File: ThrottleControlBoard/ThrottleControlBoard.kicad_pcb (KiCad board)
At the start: 2 copper layers, 95.1 x 65.7 mm, 48 parts, among them J1 BTS7960 module, J10 Conn_02x25_Odd_Even, J2 e-Throttle, J3 Conn_01x14, J4 TB TPS, J5 5V, J6 Conn_02x25_Odd_Even, J7 Conn_02x25_Odd_Even, SW2 SW_SPDT, U1 PCA9685PW

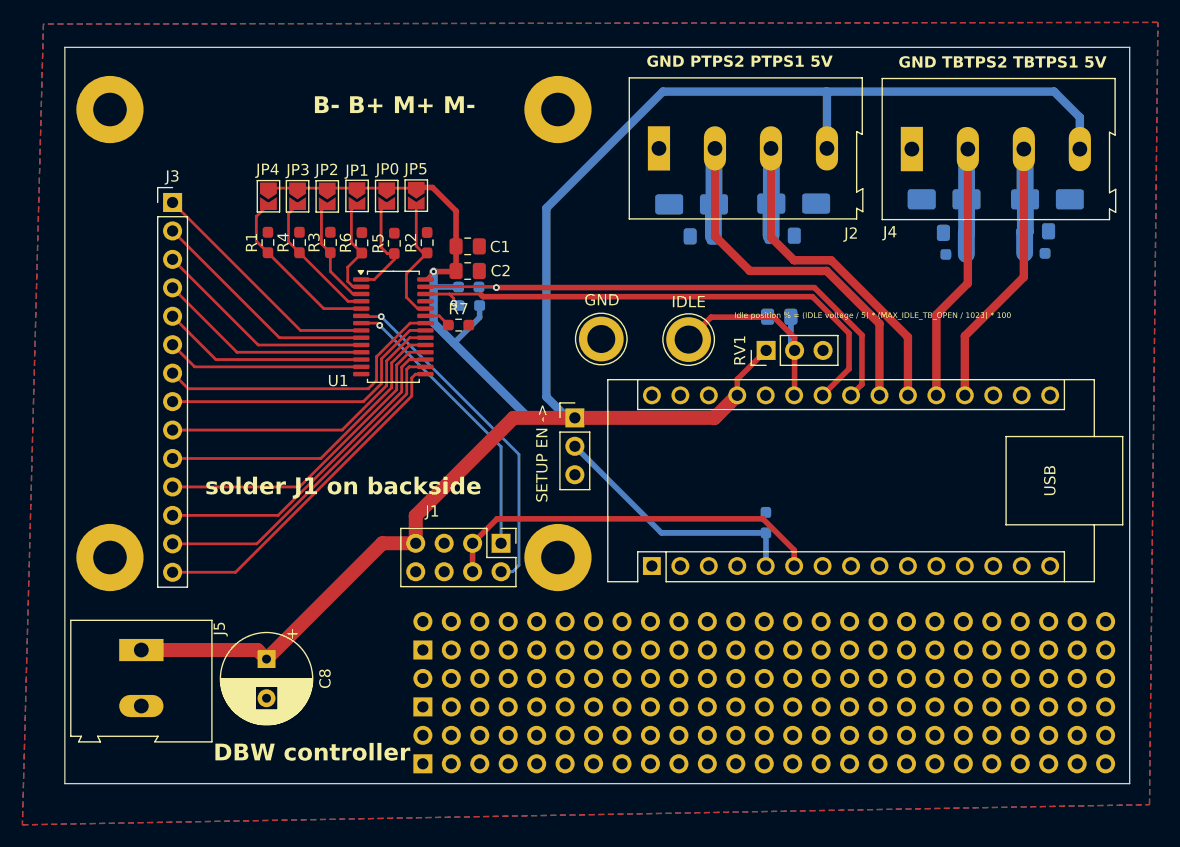
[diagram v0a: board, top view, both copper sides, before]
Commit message: DRC and vias fixed
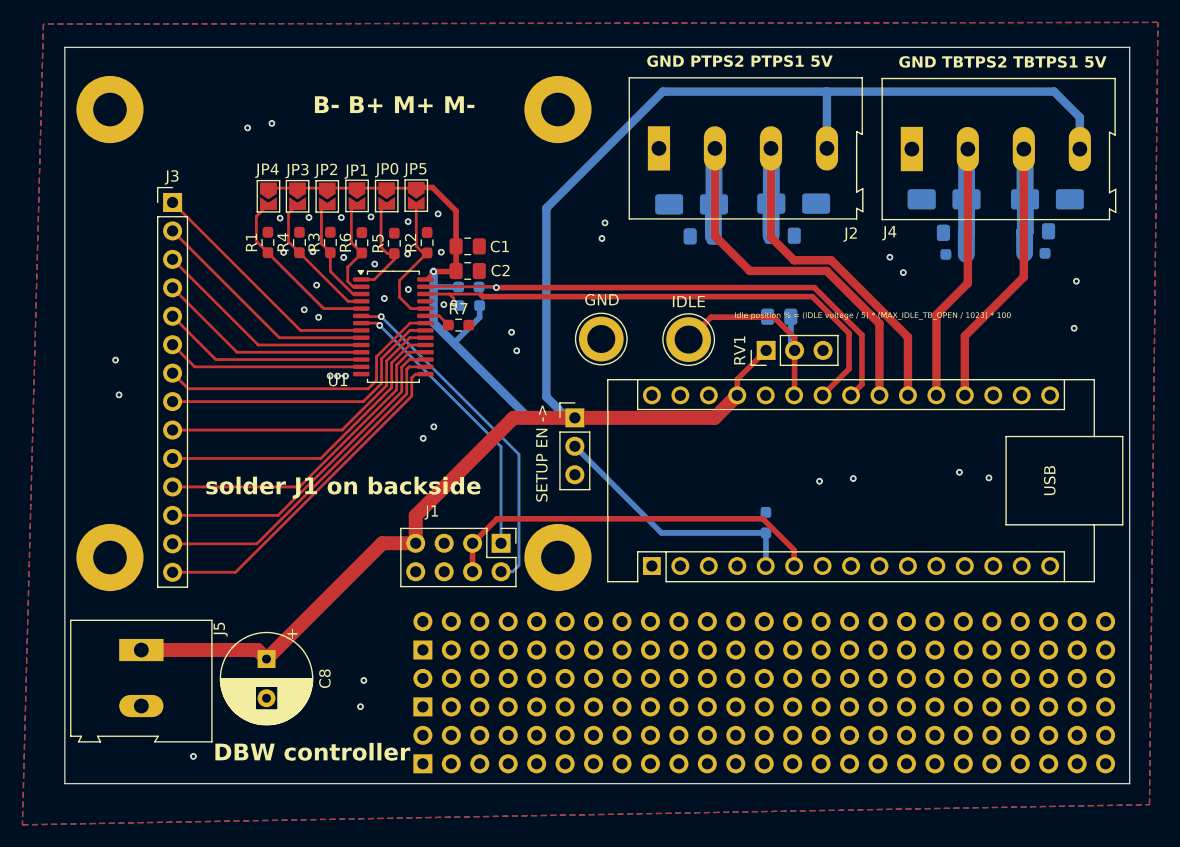
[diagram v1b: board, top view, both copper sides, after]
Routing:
- net Net-(JP5-B): track 11.9 -> 12.7 mm
- net GND: vias 0 -> 42
